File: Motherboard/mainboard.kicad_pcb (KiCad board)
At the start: 4 copper layers, 45 x 35 mm, 44 parts, among them IC1 BMX160, J1 Conn_01x01, J2 10118194-0001LF, J28 Conn_01x01, J29 Conn_01x01, J3 Micro_SD_Card, J30 Conn_01x01, J4 xf2m-2415-1a, J5 XF2M-1015-1A, SW1 KMR231NG LFS, U1 RFM95W-915S2, U2 ATSAMD51G_TQFN48, U3 DRV8848, U4 TPS82740BSIPR, U5 DRV8848, U6 MAX708RESA-T, U8 RFM95W-915S2, X1 ANTENNA_U.FL, X2 ANTENNA_U.FL

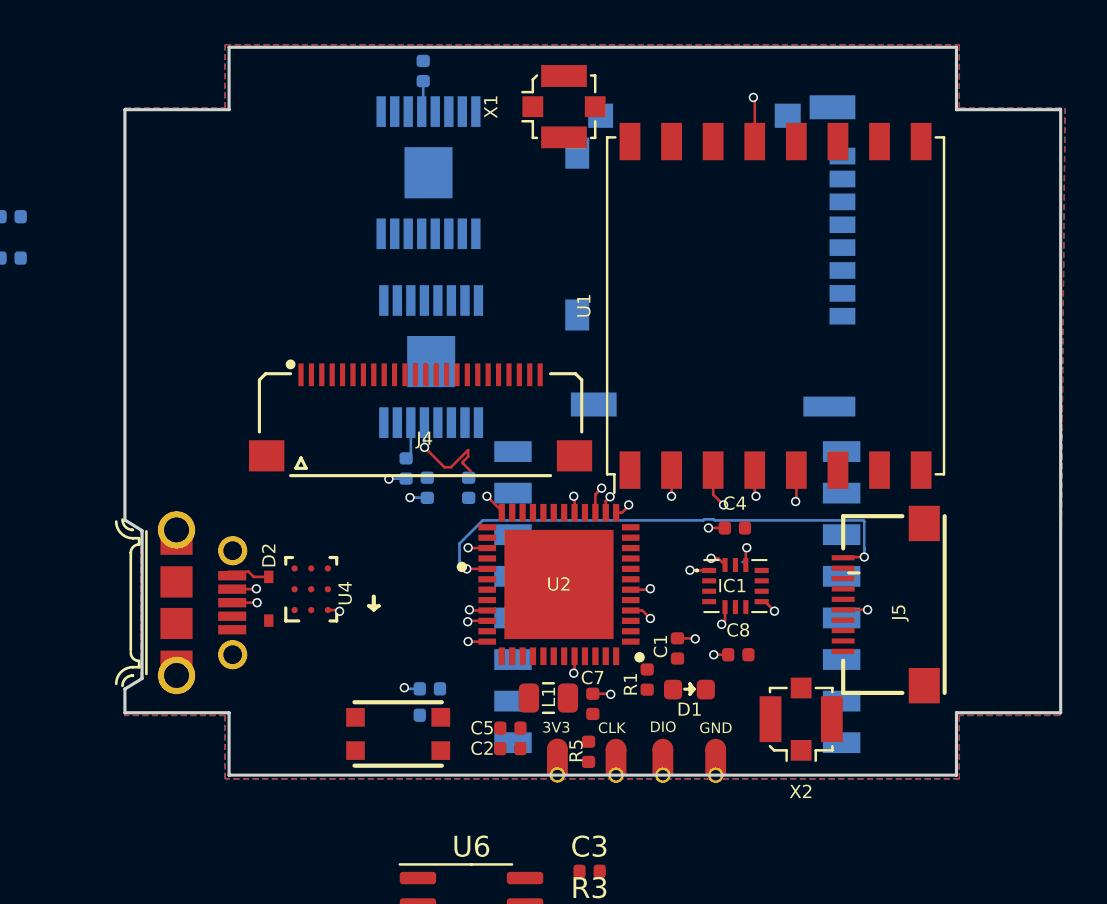
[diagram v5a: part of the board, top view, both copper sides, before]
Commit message: updated camera connector and connected to MCU and flat flex connector
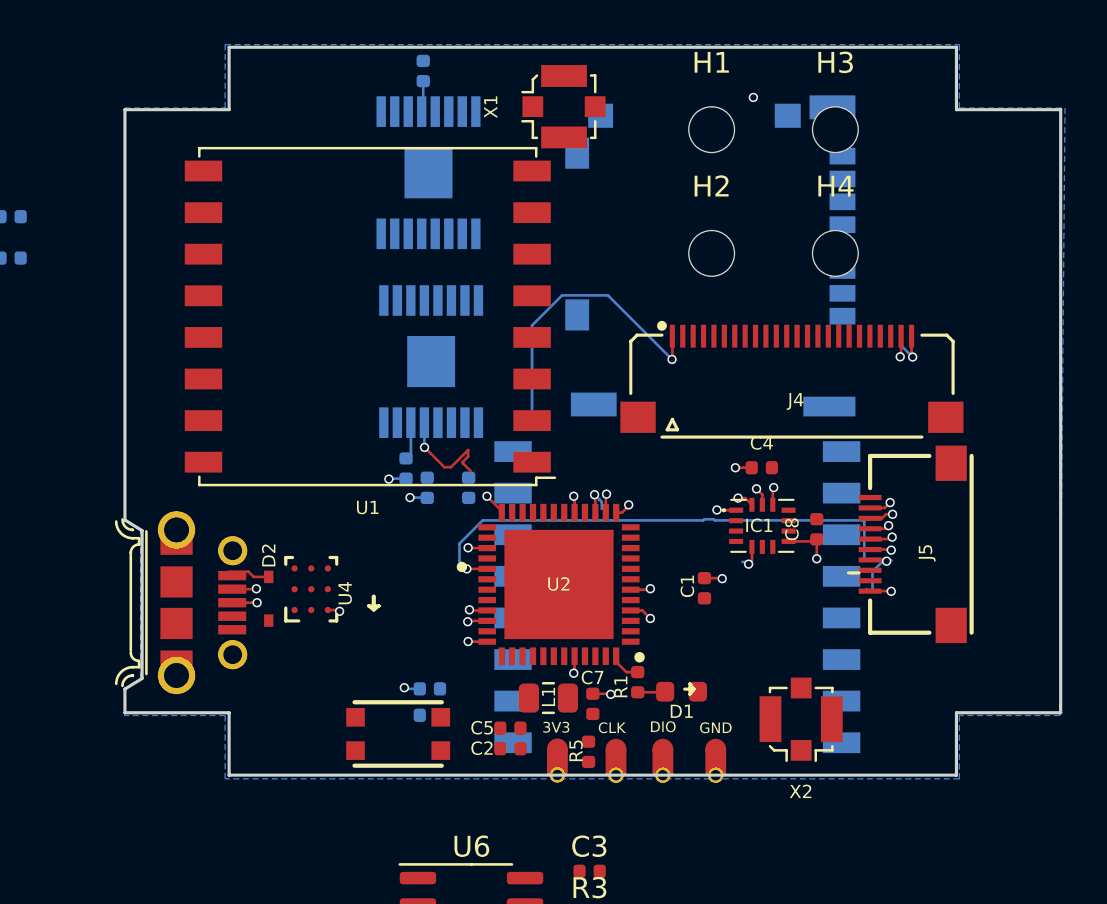
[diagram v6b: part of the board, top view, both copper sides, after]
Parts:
- added H1: MountingHole, MountingHole:MountingHole_2.2mm_M2, F.Cu at (104.9, 78.0)
- added H2: MountingHole, MountingHole:MountingHole_2.2mm_M2, F.Cu at (104.9, 84.0)
- added H3: MountingHole, MountingHole:MountingHole_2.2mm_M2, F.Cu at (110.9, 78.0)
- added H4: MountingHole, MountingHole:MountingHole_2.2mm_M2, F.Cu at (110.9, 84.0)
- moved U1 19.6 mm to (88.4, 87.0), turned to 180 degrees
- moved J4 18.0 mm to (108.8, 87.9)
- moved C8 7.11 mm to (110.0, 97.2), turned to 90 degrees
- moved C1 3.17 mm to (104.6, 100.1)
- moved C4 3.17 mm to (107.3, 94.3)
- moved IC1 3.17 mm to (107.4, 97.1)
- moved J5 3.17 mm to (112.5, 97.9)
- moved R1 0.47 mm to (101.4, 104.6)
- moved D1 0.39 mm to (103.5, 105.0)
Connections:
- J4 pad 23: Net-(J4-Pad23) -> BATT_N
- J4 pad 24: Net-(J4-Pad24) -> BATT_P
- J4 pad 5: BATT_P -> Net-(J4-Pad5)
- J4 pad 7: BATT_N -> Net-(J4-Pad7)
- J5 pad 10: EN_CAM -> Net-(J5-Pad10)
- J5 pad 3: MOSI -> Net-(J5-Pad3)
- J5 pad 5: CS_CAM -> EN_CAM
- J5 pad 6: Net-(J5-Pad6) -> CS_CAM
- J5 pad 8: Net-(J5-Pad8) -> MOSI
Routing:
- net EN_CAM: track 25.1 -> 45.9 mm
- net CS_CAM: track 2.26 -> 22.5 mm
- net 3V3: track 0.00 -> 14.8 mm, vias 0 -> 1
- net BATT_P: track 0.00 -> 14.5 mm, vias 0 -> 2
- net BATT_N: track 0.00 -> 14.4 mm, vias 0 -> 2
- net CS_IMU: track 15.2 -> 1.77 mm
- net SCK: track 9.67 -> 16.9 mm, vias 2 -> 3
- net /USB-: track 6.99 -> 2.04 mm
- net MOSI: track 11.1 -> 15.9 mm
- net /USB+: track 6.95 -> 2.33 mm
- net CS_RF2: track 1.53 -> 0.00 mm, vias 1 -> 0
- net /LED1: track 0.00 -> 1.51 mm
- net Net-(D1-Pad1): track 0.00 -> 1.33 mm
- net +3V3: track 12.5 -> 11.4 mm, vias 13 -> 12
- net MISO: track 11.6 -> 12.5 mm
- removed copper zone on F.Cu, net GND

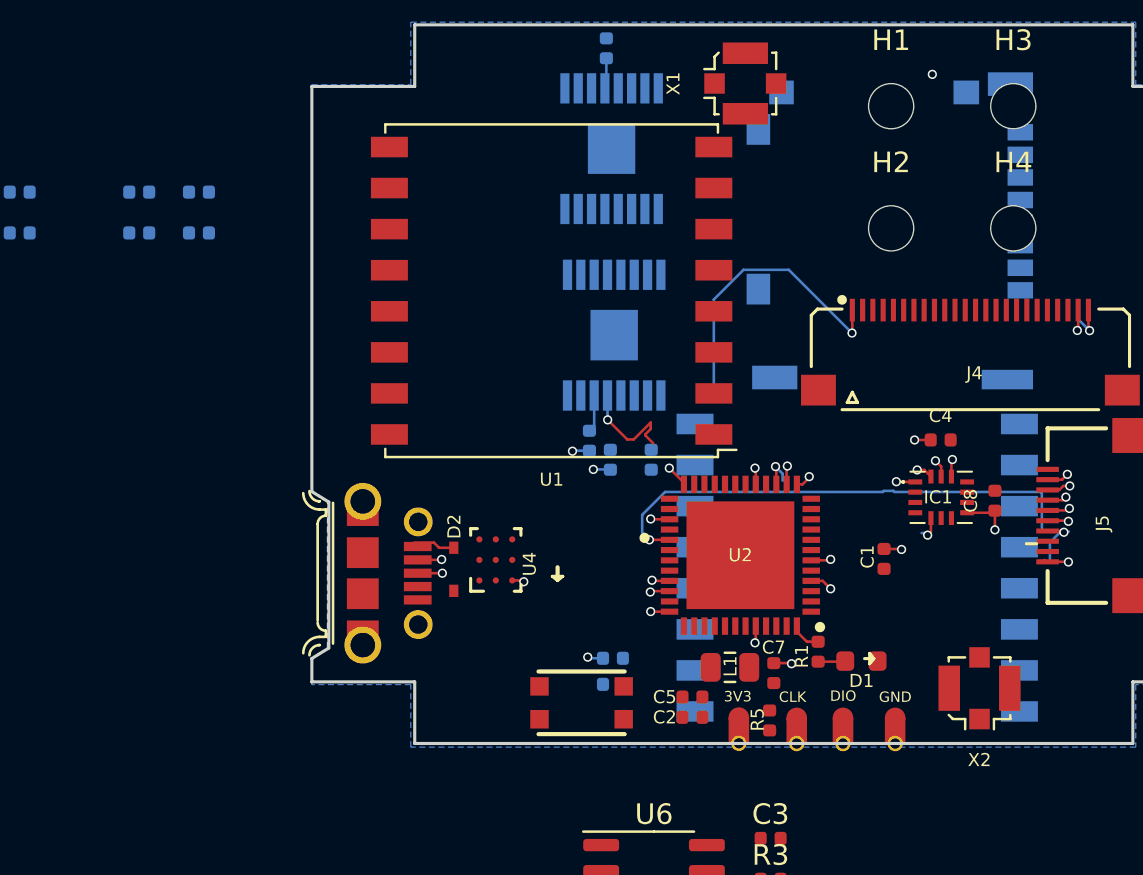
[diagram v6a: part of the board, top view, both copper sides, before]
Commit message: added vias to flat flex connector, added traces to comm protocols off of MCU
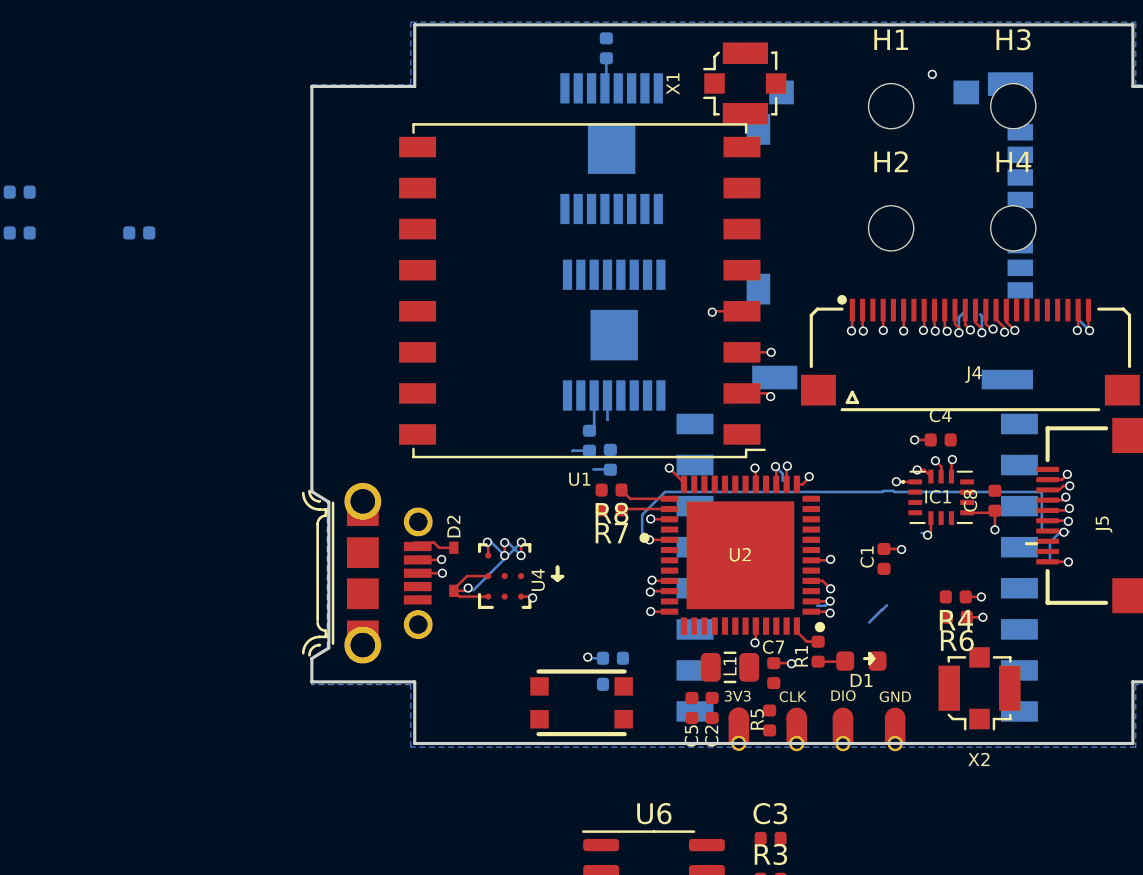
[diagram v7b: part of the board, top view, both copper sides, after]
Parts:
- R4, R6, R7, R8: moved to F.Cu
- moved R6 41.4 mm to (108.1, 102.9), turned to 180 degrees
- moved R7 27.7 mm to (91.3, 97.7), turned to 180 degrees
- moved R8 24.8 mm to (91.3, 96.7), turned to 180 degrees
- moved R4 16.3 mm to (108.1, 101.9), turned to 180 degrees
- moved U1 1.37 mm to (89.8, 87.0)
- moved C2 1.06 mm to (96.2, 107.3), turned to 270 degrees
- moved U4 0.90 mm to (86.1, 100.9)
- moved C5 0.53 mm to (95.2, 107.3), turned to 270 degrees
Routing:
- net Net-(D2-Pad1): track 0.00 -> 23.2 mm, vias 0 -> 6
- net SCK: track 16.9 -> 32.3 mm, vias 3 -> 4
- net 3V3: track 14.8 -> 1.03 mm
- net SCL1: track 0.00 -> 12.0 mm, vias 0 -> 3
- net SDA1: track 0.00 -> 11.7 mm, vias 0 -> 3
- net MOSI: track 15.9 -> 24.1 mm, vias 3 -> 4
- net MISO: track 12.5 -> 17.4 mm, vias 3 -> 4
- net GND: track 7.74 -> 3.63 mm, vias 4 -> 1
- net SCL2: track 0.00 -> 3.65 mm, vias 0 -> 1
- net SDA2: track 0.00 -> 3.51 mm, vias 0 -> 1
- net BURN2: track 0.00 -> 2.37 mm, vias 0 -> 1
- net COIL3P: track 0.00 -> 1.08 mm, vias 0 -> 1
- net COIL3N: track 0.00 -> 1.07 mm, vias 0 -> 1
- net BURN1: track 0.00 -> 1.04 mm, vias 0 -> 1
- net COIL1P: track 0.00 -> 1.04 mm, vias 0 -> 1
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
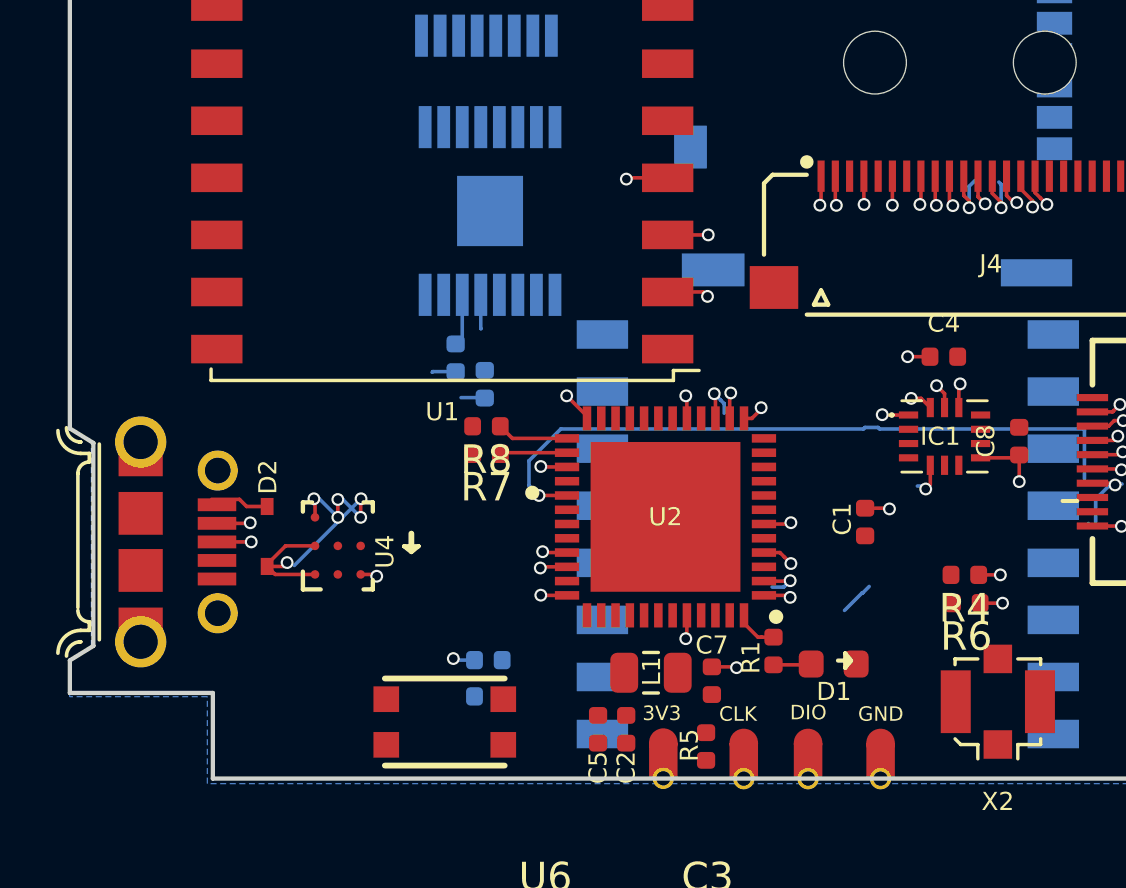
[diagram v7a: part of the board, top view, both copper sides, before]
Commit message: added WDT_WDI net to MCU, connected C2, C5, and L1 to MCU
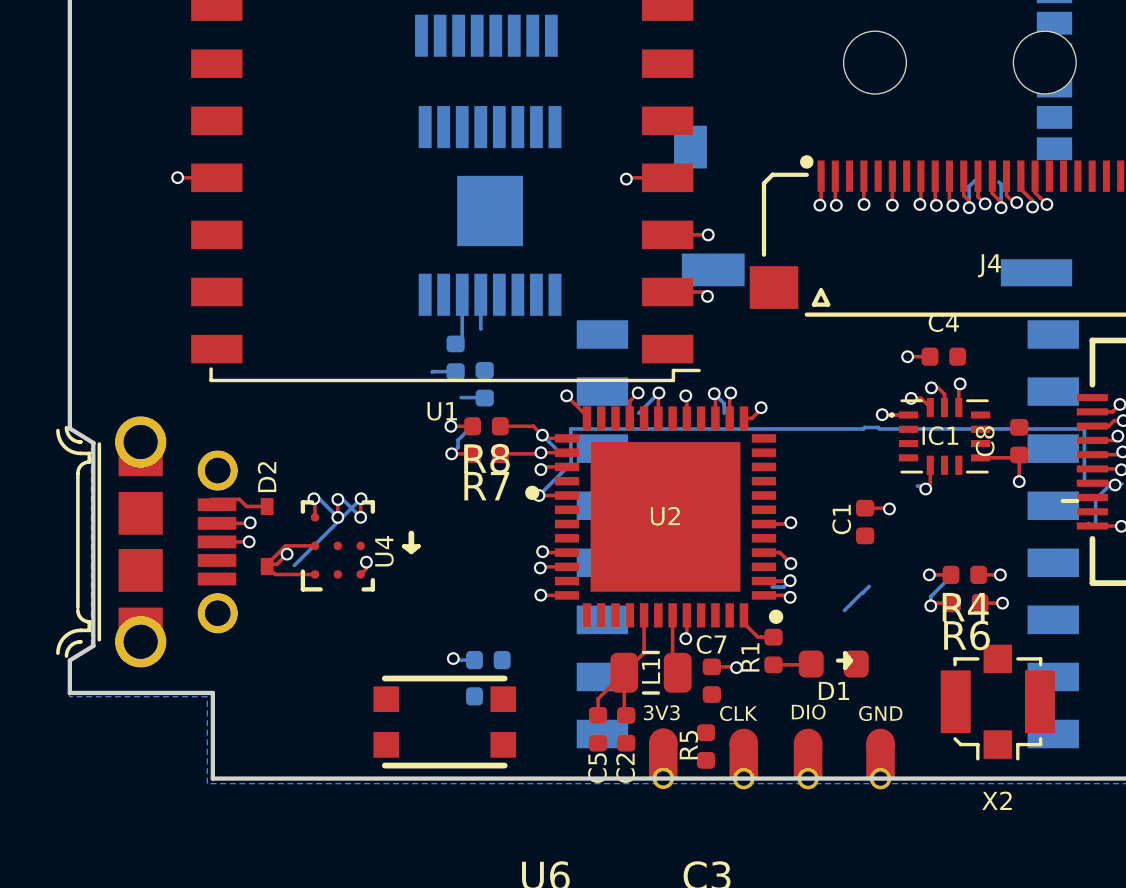
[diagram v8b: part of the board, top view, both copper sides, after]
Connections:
- J4 pad 13: SCL1 -> SCL2
- J4 pad 14: SCL2 -> SDA2
- J4 pad 15: SDA1 -> SCL1
- J4 pad 16: SDA2 -> SDA1
- U2 pad 20: Net-(U2-Pad20) -> WDT_WDI
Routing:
- net CS_IMU: track 1.77 -> 19.8 mm
- net SDA1: track 11.7 -> 27.4 mm
- net SCL1: track 12.0 -> 25.4 mm
- net /USB-: track 2.04 -> 13.6 mm
- net /USB+: track 2.15 -> 12.9 mm
- net +3V3: track 11.4 -> 18.4 mm, vias 12 -> 17
- net Net-(C2-Pad1): track 0.00 -> 5.70 mm
- net Net-(D2-Pad1): track 23.2 -> 20.4 mm
- net Net-(L1-Pad1): track 0.00 -> 2.09 mm
- net RF_CS: track 0.00 -> 1.91 mm, vias 0 -> 1
- net SCL2: track 3.65 -> 5.49 mm, vias 1 -> 2
- net RF_RST: track 0.00 -> 1.24 mm, vias 0 -> 1
- net SDA2: track 3.51 -> 3.55 mm, vias 1 -> 2
